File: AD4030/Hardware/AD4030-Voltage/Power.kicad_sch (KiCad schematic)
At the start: 48 parts, among them J501 1715721, Q501 SI5618A, Q502 MMBT3904, U501 TPS65133DPDR, U502 TSR_1-2433, U503 TEC3-2419WI, U504 LT1763CDE-ADJ, U505 LT1763CDE-1.8, U506 LT1763IDE-3.3, U508 TSR_1-2450

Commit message: Hardware design
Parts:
- C515: value 47u/25V -> 2u2; footprint Capacitor_SMD:C_1210_3225Metric_Pad1.33x2.70mm_HandSolder -> Capacitor_SMD:C_0805_2012Metric_Pad1.18x1.45mm_HandSolder
- FB501, FB502: value BLM31PG330SN1L -> FBMJ2125HM330-T; footprint Inductor_SMD:L_1206_3216Metric_Pad1.22x1.90mm_HandSolder -> Inductor_SMD:L_0805_2012Metric_Pad1.15x1.40mm_HandSolder
- L501, L502, L505, L506: value XFL4020-472MEC -> 1239AS-H-4R7M; footprint Inductor_SMD:L_Coilcraft_XxL4020 -> Inductor_SMD:L_1008_2520Metric_Pad1.43x2.20mm_HandSolder
- renumbered C517 to C516, C516 to C517, U508 to U507
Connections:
- net GNDS: now also J501.2 (Pin_2), R501.2, R502.2
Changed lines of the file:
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@@
 	)
 	(junction
+		(at 31.75 45.72)
+		(diameter 0)
+		(color 0 0 0 0)
+	)
+	(junction
 		(at 224.79 153.67)
 		(diameter 0)
@@
 	(wire
 		(pts
+			(xy 31.75 45.72) (xy 31.75 46.99)
+		)
+		(stroke
+			(width 0)
+			(type default)
+		)
+	)
+	(wire
+		(pts
 			(xy 125.73 72.39) (xy 121.92 72.39)
 		)
@@
 			)
 		)
-		(property "Value" "XFL4020-472MEC"
+		(property "Value" "1239AS-H-4R7M"
 			(at 52.07 133.35 90)
 			(effects
@@
 			)
 		)
-		(property "Footprint" "Inductor_SMD:L_Coilcraft_XxL4020"
+		(property "Footprint" "Inductor_SMD:L_1008_2520Metric_Pad1.43x2.20mm_HandSolder"
 			(at 52.07 135.89 0)
 			(effects
@@
 			)
 		)
-		(property "Value" "47u/25V"
+		(property "Value" "2u2"
 			(at 224.79 33.0199 0)
 			(effects
@@
 			)
 		)
-		(property "Footprint" "Capacitor_SMD:C_1210_3225Metric_Pad1.33x2.70mm_HandSolder"
+		(property "Footprint" "Capacitor_SMD:C_0805_2012Metric_Pad1.18x1.45mm_HandSolder"
 			(at 221.9452 35.56 0)
 			(effects
@@
 	(symbol
 		(lib_id "power:GNDS")
+		(at 31.75 46.99 0)
+		(unit 1)
+		(exclude_from_sim no)
+		(in_bom yes)
+		(on_board yes)
+		(dnp no)
+		(property "Reference" "#PWR0531"
+			(at 31.75 53.34 0)
+			(effects
+				(font
+					(size 1.27 1.27)
+				)
+				(hide yes)
+			)
+		)
+		(property "Value" "GNDS"
+			(at 31.75 51.054 0)
+			(effects
+				(font
+					(size 1.27 1.27)
+				)
+			)
+		)
+		(property "Footprint" ""
+			(at 31.75 46.99 0)
+			(effects
+				(font
+					(size 1.27 1.27)
+				)
+				(hide yes)
+			)
+		)
+		(property "Datasheet" ""
+			(at 31.75 46.99 0)
+			(effects
+				(font
+					(size 1.27 1.27)
+				)
+				(hide yes)
+			)
+		)
+		(property "Description" "Power symbol creates a global label with name \"GNDS\" , signal ground"
+			(at 31.75 46.99 0)
+			(effects
+				(font
+					(size 1.27 1.27)
+				)
+				(hide yes)
+			)
+		)
+		(pin "1"
+		)
+		(instances
+			(project "AD4030-Voltage"
+				(path "/af28bfe6-a5ae-47dd-9259-97a6edcec559/f42c105e-3e32-408a-b35b-b6040745c080"
+					(reference "#PWR0531")
+					(unit 1)
+				)
+			)
+		)
+	)
+	(symbol
+		(lib_id "power:GNDS")
 		(at 125.73 83.82 0)
 		(unit 1)
@@
 		(on_board yes)
 		(dnp no)
-		(property "Reference" "C517"
+		(property "Reference" "C516"
 			(at 238.76 147.32 0)
 			(effects
@@
 			(project "AD4030-Voltage"
 				(path "/af28bfe6-a5ae-47dd-9259-97a6edcec559/f42c105e-3e32-408a-b35b-b6040745c080"
-					(reference "C517")
+					(reference "C516")
 					(unit 1)
 				)
@@
 		(dnp no)
 		(fields_autoplaced yes)
-		(property "Reference" "#PWR0527"
+		(property "Reference" "#PWR0526"
 			(at 236.22 146.05 0)
 			(effects
@@
 			(project ""
 				(path "/af28bfe6-a5ae-47dd-9259-97a6edcec559/f42c105e-3e32-408a-b35b-b6040745c080"
-					(reference "#PWR0527")
+					(reference "#PWR0526")
 					(unit 1)
 				)
@@
 			)
 		)
-		(property "Value" "BLM31PG330SN1L"
+		(property "Value" "FBMJ2125HM330-T"
 			(at 198.0819 63.5 90)
 			(effects
@@
 			)
 		)
-		(property "Footprint" "Inductor_SMD:L_1206_3216Metric_Pad1.22x1.90mm_HandSolder"
+		(property "Footprint" "Inductor_SMD:L_0805_2012Metric_Pad1.15x1.40mm_HandSolder"
 			(at 198.12 69.088 90)
 			(effects
@@
 		(dnp no)
 		(fields_autoplaced yes)
-		(property "Reference" "U508"
+		(property "Reference" "U507"
 			(at 224.79 135.89 0)
 			(effects
@@
 			(project "AD4030-Voltage"
 				(path "/af28bfe6-a5ae-47dd-9259-97a6edcec559/f42c105e-3e32-408a-b35b-b6040745c080"
-					(reference "U508")
+					(reference "U507")
 					(unit 1)
 				)
@@
 			)
 		)
-		(property "Value" "BLM31PG330SN1L"
+		(property "Value" "FBMJ2125HM330-T"
 			(at 198.0819 101.6 90)
 			(effects
@@
 			)
 		)
-		(property "Footprint" "Inductor_SMD:L_1206_3216Metric_Pad1.22x1.90mm_HandSolder"
+		(property "Footprint" "Inductor_SMD:L_0805_2012Metric_Pad1.15x1.40mm_HandSolder"
 			(at 198.12 107.188 90)
 			(effects
@@
 		(dnp no)
 		(fields_autoplaced yes)
-		(property "Reference" "#PWR0526"
+		(property "Reference" "#PWR0527"
 			(at 237.49 25.4 0)
 			(effects
@@
 			(project "AD4030-Voltage"
 				(path "/af28bfe6-a5ae-47dd-9259-97a6edcec559/f42c105e-3e32-408a-b35b-b6040745c080"
-					(reference "#PWR0526")
+					(reference "#PWR0527")
 					(unit 1)
 				)
@@
 			)
 		)
-		(property "Value" "XFL4020-472MEC"
+		(property "Value" "1239AS-H-4R7M"
 			(at 130.81 127 90)
 			(effects
@@
 			)
 		)
-		(property "Footprint" "Inductor_SMD:L_Coilcraft_XxL4020"
+		(property "Footprint" "Inductor_SMD:L_1008_2520Metric_Pad1.43x2.20mm_HandSolder"
 			(at 130.81 129.54 0)
 			(effects
@@
 		(dnp no)
 		(fields_autoplaced yes)
-		(property "Reference" "C516"
+		(property "Reference" "C517"
 			(at 241.3 30.4799 0)
 			(effects
@@
 			(project ""
 				(path "/af28bfe6-a5ae-47dd-9259-97a6edcec559/f42c105e-3e32-408a-b35b-b6040745c080"
-					(reference "C516")
+					(reference "C517")
 					(unit 1)
 				)
@@
 			)
 		)
-		(property "Value" "XFL4020-472MEC"
+		(property "Value" "1239AS-H-4R7M"
 			(at 129.54 152.4 90)
 			(effects
@@
 			)
 		)
-		(property "Footprint" "Inductor_SMD:L_Coilcraft_XxL4020"
+		(property "Footprint" "Inductor_SMD:L_1008_2520Metric_Pad1.43x2.20mm_HandSolder"
 			(at 129.54 149.86 0)
 			(effects
@@
 			)
 		)
-		(property "Value" "XFL4020-472MEC"
+		(property "Value" "1239AS-H-4R7M"
 			(at 96.52 146.05 90)
 			(effects
@@
 			)
 		)
-		(property "Footprint" "Inductor_SMD:L_Coilcraft_XxL4020"
+		(property "Footprint" "Inductor_SMD:L_1008_2520Metric_Pad1.43x2.20mm_HandSolder"
 			(at 96.52 148.59 0)
 			(effects

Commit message: PCB layout
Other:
- moved on the sheet: C521, C523
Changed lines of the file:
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@@
 	)
 	(junction
-		(at 254 67.31)
+		(at 252.73 67.31)
 		(diameter 0)
 		(color 0 0 0 0)
@@
 	)
 	(junction
-		(at 269.24 67.31)
+		(at 267.97 67.31)
 		(diameter 0)
 		(color 0 0 0 0)
@@
 	)
 	(junction
-		(at 254 83.82)
+		(at 252.73 83.82)
 		(diameter 0)
 		(color 0 0 0 0)
@@
 	(wire
 		(pts
-			(xy 269.24 67.31) (xy 269.24 72.39)
+			(xy 267.97 67.31) (xy 267.97 72.39)
 		)
 		(stroke
@@
 	(wire
 		(pts
-			(xy 254 83.82) (xy 224.79 83.82)
+			(xy 252.73 83.82) (xy 224.79 83.82)
 		)
 		(stroke
@@
 	(wire
 		(pts
-			(xy 254 66.04) (xy 254 67.31)
+			(xy 252.73 66.04) (xy 252.73 67.31)
 		)
 		(stroke
@@
 	(wire
 		(pts
-			(xy 269.24 80.01) (xy 269.24 83.82)
+			(xy 267.97 80.01) (xy 267.97 83.82)
 		)
 		(stroke
@@
 	(wire
 		(pts
-			(xy 254 67.31) (xy 269.24 67.31)
+			(xy 252.73 67.31) (xy 267.97 67.31)
 		)
 		(stroke
@@
 	(wire
 		(pts
-			(xy 269.24 66.04) (xy 269.24 67.31)
+			(xy 267.97 66.04) (xy 267.97 67.31)
 		)
 		(stroke
@@
 	(wire
 		(pts
-			(xy 254 83.82) (xy 269.24 83.82)
+			(xy 252.73 83.82) (xy 267.97 83.82)
 		)
 		(stroke
@@
 	(wire
 		(pts
-			(xy 254 80.01) (xy 254 83.82)
+			(xy 252.73 80.01) (xy 252.73 83.82)
 		)
 		(stroke
@@
 	(wire
 		(pts
-			(xy 241.3 67.31) (xy 254 67.31)
+			(xy 241.3 67.31) (xy 252.73 67.31)
 		)
 		(stroke
@@
 	(wire
 		(pts
-			(xy 254 72.39) (xy 254 67.31)
+			(xy 252.73 72.39) (xy 252.73 67.31)
 		)
 		(stroke
@@
 	(symbol
 		(lib_id "Device:C")
-		(at 269.24 76.2 0)
+		(at 267.97 76.2 0)
 		(unit 1)
 		(exclude_from_sim no)
@@
 		(fields_autoplaced yes)
 		(property "Reference" "C523"
-			(at 273.05 74.9299 0)
+			(at 271.78 74.9299 0)
 			(effects
 				(font
@@
 		)
 		(property "Value" "10u/25V"
-			(at 273.05 77.4699 0)
+			(at 271.78 77.4699 0)
 			(effects
 				(font
@@
 		)
 		(property "Footprint" "Capacitor_SMD:C_1206_3216Metric_Pad1.33x1.80mm_HandSolder"
-			(at 270.2052 80.01 0)
+			(at 268.9352 80.01 0)
 			(effects
 				(font
@@
 		)
 		(property "Datasheet" "~"
-			(at 269.24 76.2 0)
+			(at 267.97 76.2 0)
 			(effects
 				(font
@@
 		)
 		(property "Description" "Unpolarized capacitor"
-			(at 269.24 76.2 0)
+			(at 267.97 76.2 0)
 			(effects
 				(font
@@
 		(on_board yes)
 		(dnp no)
-		(fields_autoplaced yes)
 		(property "Reference" "#PWR0523"
 			(at 224.79 91.44 0)
@@
 	(symbol
 		(lib_id "power:+1V8")
-		(at 269.24 66.04 0)
+		(at 267.97 66.04 0)
 		(unit 1)
 		(exclude_from_sim no)
@@
 		(fields_autoplaced yes)
 		(property "Reference" "#PWR0530"
-			(at 269.24 69.85 0)
+			(at 267.97 69.85 0)
 			(effects
 				(font
@@
 		)
 		(property "Value" "+1V8"
-			(at 269.24 60.96 0)
+			(at 267.97 60.96 0)
 			(effects
 				(font
@@
 		)
 		(property "Footprint" ""
-			(at 269.24 66.04 0)
+			(at 267.97 66.04 0)
 			(effects
 				(font
@@
 		)
 		(property "Datasheet" ""
-			(at 269.24 66.04 0)
+			(at 267.97 66.04 0)
 			(effects
 				(font
@@
 		)
 		(property "Description" "Power symbol creates a global label with name \"+1V8\""
-			(at 269.24 66.04 0)
+			(at 267.97 66.04 0)
 			(effects
 				(font
@@
 	(symbol
 		(lib_id "Device:C")
-		(at 254 76.2 0)
+		(at 252.73 76.2 0)
 		(unit 1)
 		(exclude_from_sim no)
@@
 		(dnp no)
 		(property "Reference" "C521"
-			(at 257.81 74.9299 0)
+			(at 256.54 74.9299 0)
 			(effects
 				(font
@@
 		)
 		(property "Value" "47u/25V"
-			(at 257.81 77.4699 0)
+			(at 256.54 77.4699 0)
 			(effects
 				(font
@@
 		)
 		(property "Footprint" "Capacitor_SMD:C_1210_3225Metric_Pad1.33x2.70mm_HandSolder"
-			(at 254.9652 80.01 0)
+			(at 253.6952 80.01 0)
 			(effects
 				(font
@@
 		)
 		(property "Datasheet" "~"
-			(at 254 76.2 0)
+			(at 252.73 76.2 0)
 			(effects
 				(font
@@
 		)
 		(property "Description" "Unpolarized capacitor"
-			(at 254 76.2 0)
+			(at 252.73 76.2 0)
 			(effects
 				(font
@@
 	(symbol
 		(lib_id "AD4030:VIO")
-		(at 254 66.04 0)
+		(at 252.73 66.04 0)
 		(unit 1)
 		(exclude_from_sim no)
@@
 		(fields_autoplaced yes)
 		(property "Reference" "#PWR0528"
-			(at 254 69.85 0)
+			(at 252.73 69.85 0)
 			(effects
 				(font
@@
 		)
 		(property "Value" "VIO"
-			(at 254 60.96 0)
+			(at 252.73 60.96 0)
 			(effects
 				(font
@@
 		)
 		(property "Footprint" ""
-			(at 254 66.04 0)
+			(at 252.73 66.04 0)
 			(effects
 				(font
@@
 		)
 		(property "Datasheet" ""
-			(at 254 66.04 0)
+			(at 252.73 66.04 0)
 			(effects
 				(font
@@
 		)
 		(property "Description" "Power symbol creates a global label with name \"VIO\""
-			(at 254 66.04 0)
+			(at 252.73 66.04 0)
 			(effects
 				(font
@@
 		(lib_id "power:+3.3V")
 		(at 267.97 104.14 0)
+		(mirror y)
 		(unit 1)
 		(exclude_from_sim no)
@@
 		(on_board yes)
 		(dnp no)
-		(fields_autoplaced yes)
 		(property "Reference" "#PWR0529"
 			(at 267.97 107.95 0)

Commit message: PCB layout
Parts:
- added D503: RED, LED_SMD:LED_0603_1608Metric, symbol Device:LED
- added R505: 680, Resistor_SMD:R_0603_1608Metric_Pad0.98x0.95mm_HandSolder, symbol Device:R
- added R506: 0, Resistor_SMD:R_0603_1608Metric_Pad0.98x0.95mm_HandSolder, symbol Device:R
- R503: value R -> 10k5
- R504: value R -> 10k
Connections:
- net +5V: now also D503.2 (A)
- net GND: now also R505.2
- net VCCQ: now also R506.2
- net at C510.1, U502.3 (Vout), U504.10 (IN)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: now also R506.1
- new net: D503.1 (K), R505.1
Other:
- moved on the sheet: C501, C502, C503, C504, C505, C506, C507, C508, C509, C510, C511, C512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

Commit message: PCB layout
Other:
- note added: "VCQQ 2V5 = R503 (10k5)/ R504 (10k) VCQQ 1V8 = R503 (4k7)/ R504 (10k)"
- moved on the sheet: C501, C502, C503, C504, C505, C506, C507, C508, C509, C510, C511, C512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

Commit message: Bug fixes in PCB.
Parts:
- U501: footprint Package_SON:WSON-12-1EP_3x3mm_P0.5mm_EP1.5x2.5mm_ThermalVias -> AD4030:DPD12_TEX
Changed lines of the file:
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@@
 			)
 		)
-		(property "Footprint" "Package_SON:WSON-12-1EP_3x3mm_P0.5mm_EP1.5x2.5mm_ThermalVias"
+		(property "Footprint" "AD4030:DPD12_TEX"
 			(at 66.04 143.51 0)
 			(effects

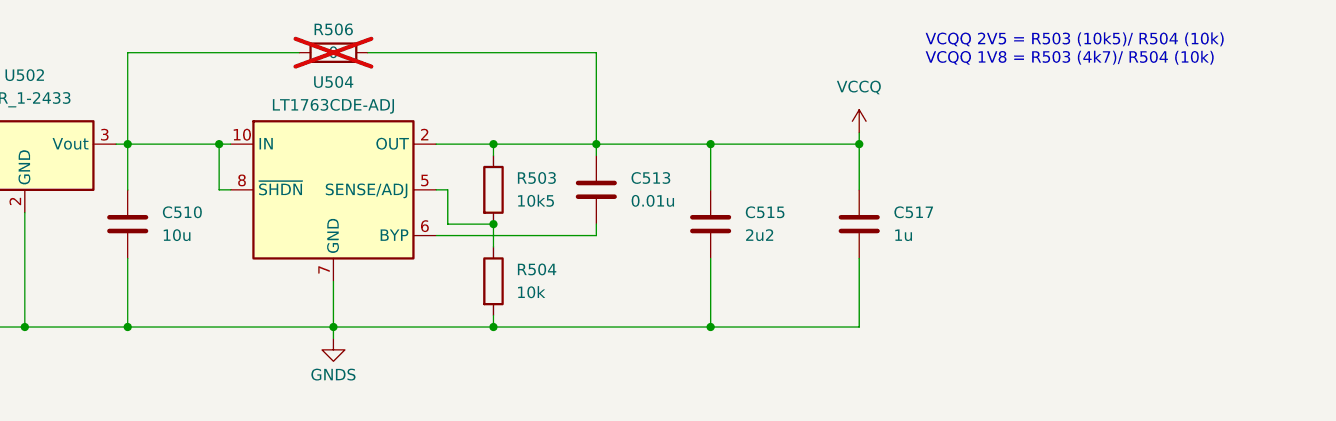
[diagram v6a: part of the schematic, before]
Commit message: AD4030-Voltage : Ordered BOM
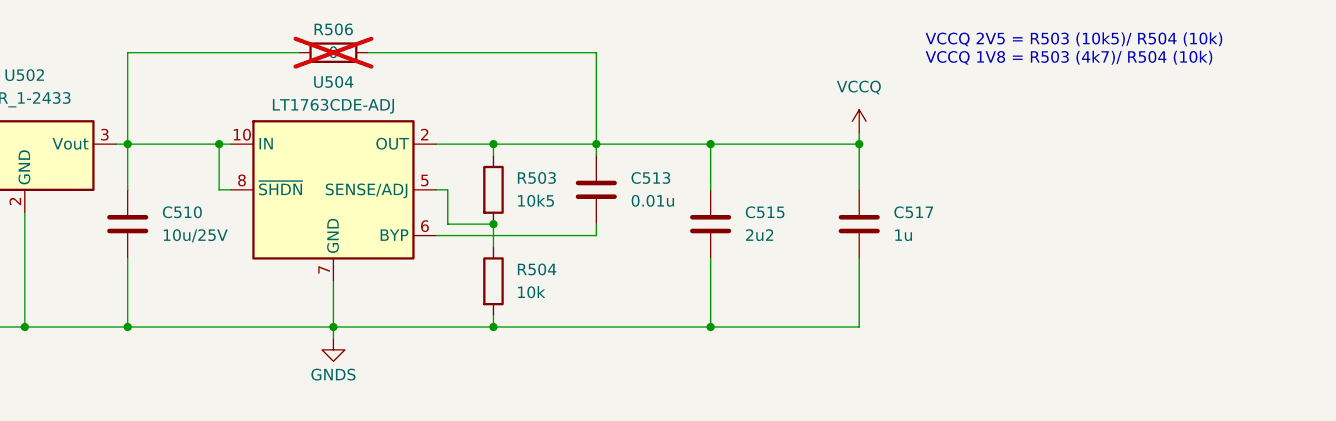
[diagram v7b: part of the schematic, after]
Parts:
- C510: value 10u -> 10u/25V
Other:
- note added: "VCCQ 2V5 = R503 (10k5)/ R504 (10k) VCCQ 1V8 = R503 (4k7)/ R504 (10k)"
- note removed: "VCQQ 2V5 = R503 (10k5)/ R504 (10k) VCQQ 1V8 = R503 (4k7)/ R504 (10k)"
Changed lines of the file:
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@@
 		)
 	)
-	(text "VCQQ 2V5 = R503 (10k5)/ R504 (10k)\nVCQQ 1V8 = R503 (4k7)/ R504 (10k)"
+	(text "VCCQ 2V5 = R503 (10k5)/ R504 (10k)\nVCCQ 1V8 = R503 (4k7)/ R504 (10k)"
 		(exclude_from_sim no)
 		(at 244.856 17.526 0)
@@
 			)
 		)
-		(property "Value" "10u"
+		(property "Value" "10u/25V"
 			(at 160.02 38.0999 0)
 			(effects
